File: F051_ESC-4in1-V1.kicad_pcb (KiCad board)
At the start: 4 copper layers, 46 x 55.8 mm, 222 parts, among them J1 Conn_01x02, J11 Conn_01x03, J14 Conn_01x03, J2 Conn_01x10, J3 Conn_01x05, J4 Conn_01x05, J5 Conn_01x05, J6 Conn_01x03, J7 Conn_01x05, J8 Conn_01x03, J9 Conn_01x10, Q1 TPHR8504PL, Q10 TPHR8504PL, Q11 TPHR8504PL, Q12 TPHR8504PL, Q13 TPHR8504PL, Q14 TPHR8504PL, Q15 TPHR8504PL, Q16 TPHR8504PL, Q17 TPHR8504PL, Q18 TPHR8504PL, Q19 TPHR8504PL, Q2 TPHR8504PL, Q20 TPHR8504PL, Q21 TPHR8504PL, Q22 TPHR8504PL, Q23 TPHR8504PL, Q24 TPHR8504PL, Q3 TPHR8504PL, Q4 TPHR8504PL, Q5 TPHR8504PL, Q6 TPHR8504PL, Q7 TPHR8504PL, Q8 TPHR8504PL, Q9 TPHR8504PL, U1 STM32F051K6Ux, U10 FD6288Q, U11 STM32F051K6Ux, U12 FD6288Q, U13 L78L12_SOT89, U14 MP4560_QFN10, U2 FD6288Q, U3 L78L12_SOT89, U4 LP2985-3.3, U5 INA139, U6 FD6288Q, U7 OPA340NA, U8 STM32F051K6Ux, U9 STM32F051K6Ux

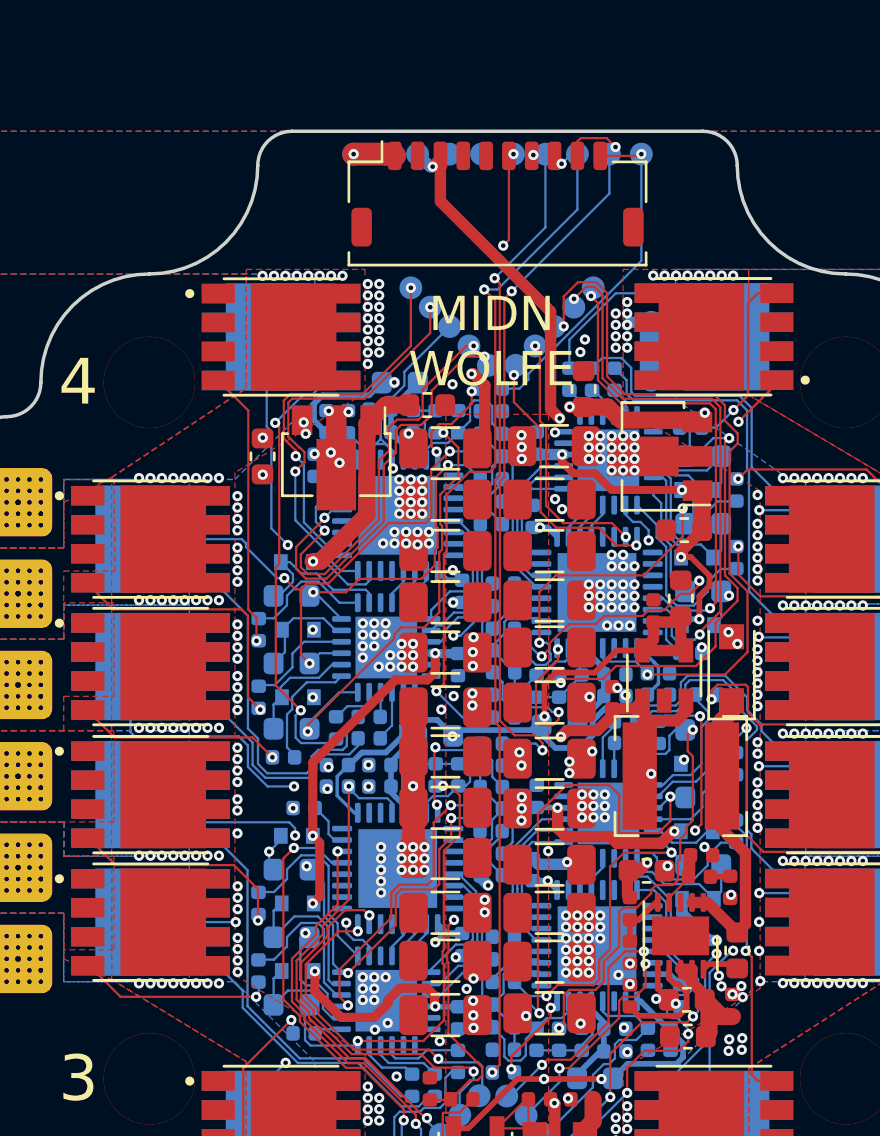
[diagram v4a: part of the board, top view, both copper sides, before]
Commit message: Some graphical additions
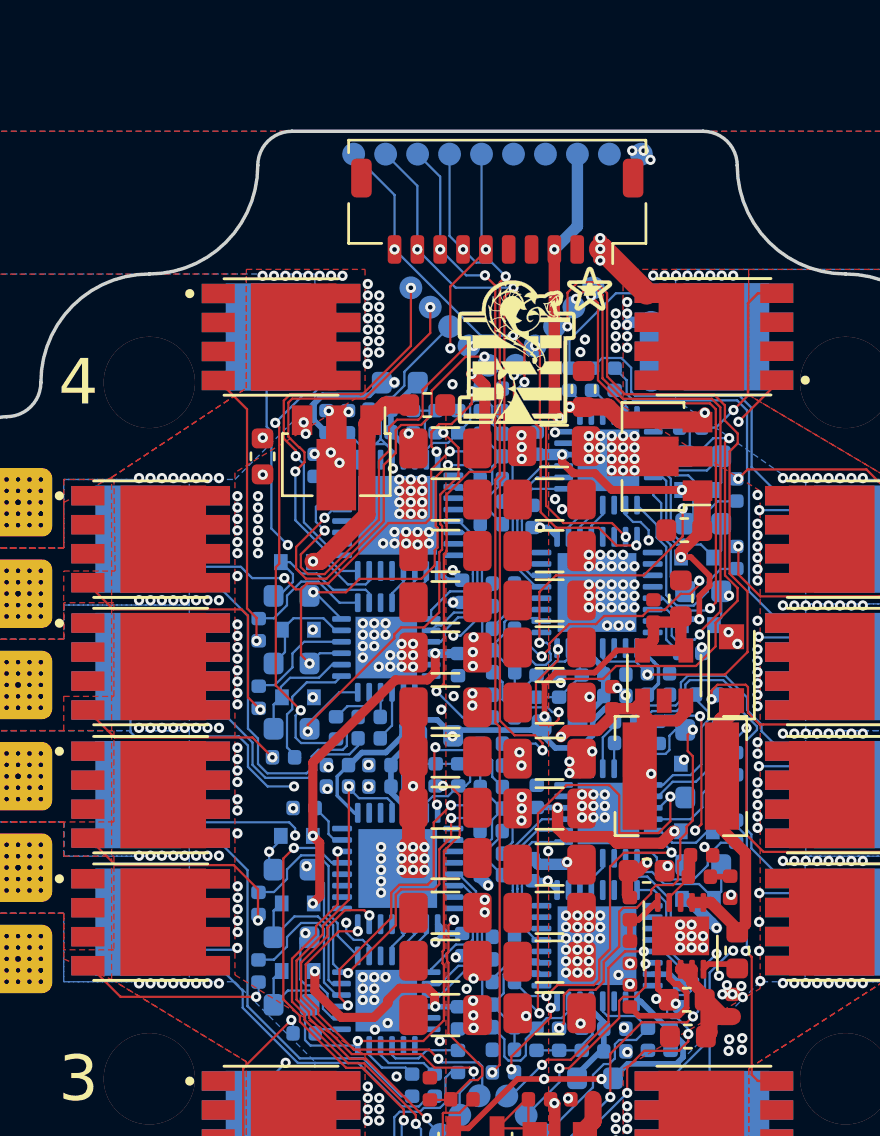
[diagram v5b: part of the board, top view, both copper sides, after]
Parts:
- added G***: LOGO, Footprints:DTOM, F.Cu at (141.6, 72.6)
- moved J2 0.75 mm to (140.0, 65.8), turned to 180 degrees
- turned J9 to 180 degrees
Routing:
- net +5V: track 48.8 -> 45.8 mm
- net /PWM_2: track 31.6 -> 29.9 mm
- net +12V_2: track 29.0 -> 27.9 mm
- net VCC_Shunt: track 20.6 -> 21.6 mm, vias 219 -> 224
- net /PWM_3: track 34.2 -> 33.3 mm
- net /MCU 3/PhaseB: track 26.6 -> 27.2 mm
- net /PWM_4: track 15.1 -> 15.0 mm, vias 1 -> 3
- net GND: vias 334 -> 349
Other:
- board text added: "CLK"
- board text added: "DIO"
- board text added: "NRST"
- board text added: "RX"
- board text added: "TX"

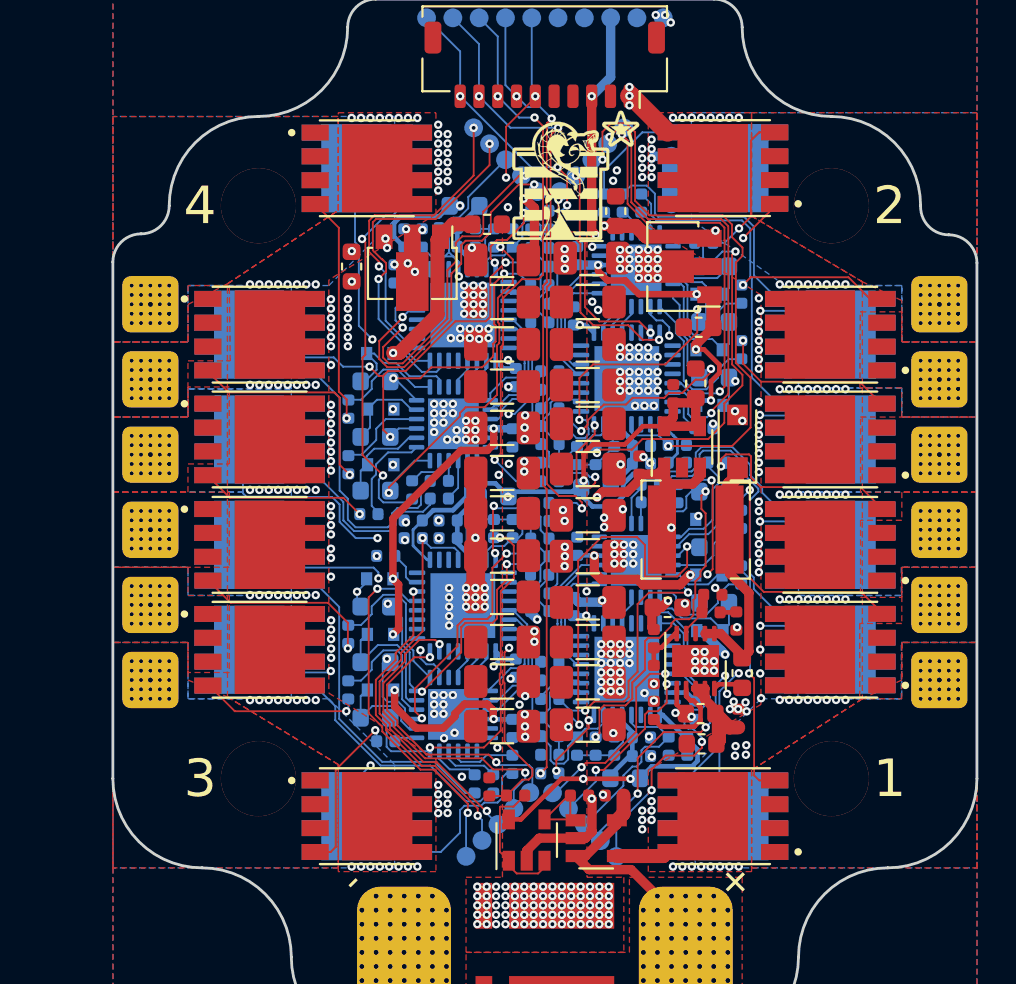
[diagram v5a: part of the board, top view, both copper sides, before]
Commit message: Adjusted some of the fills to match the grid
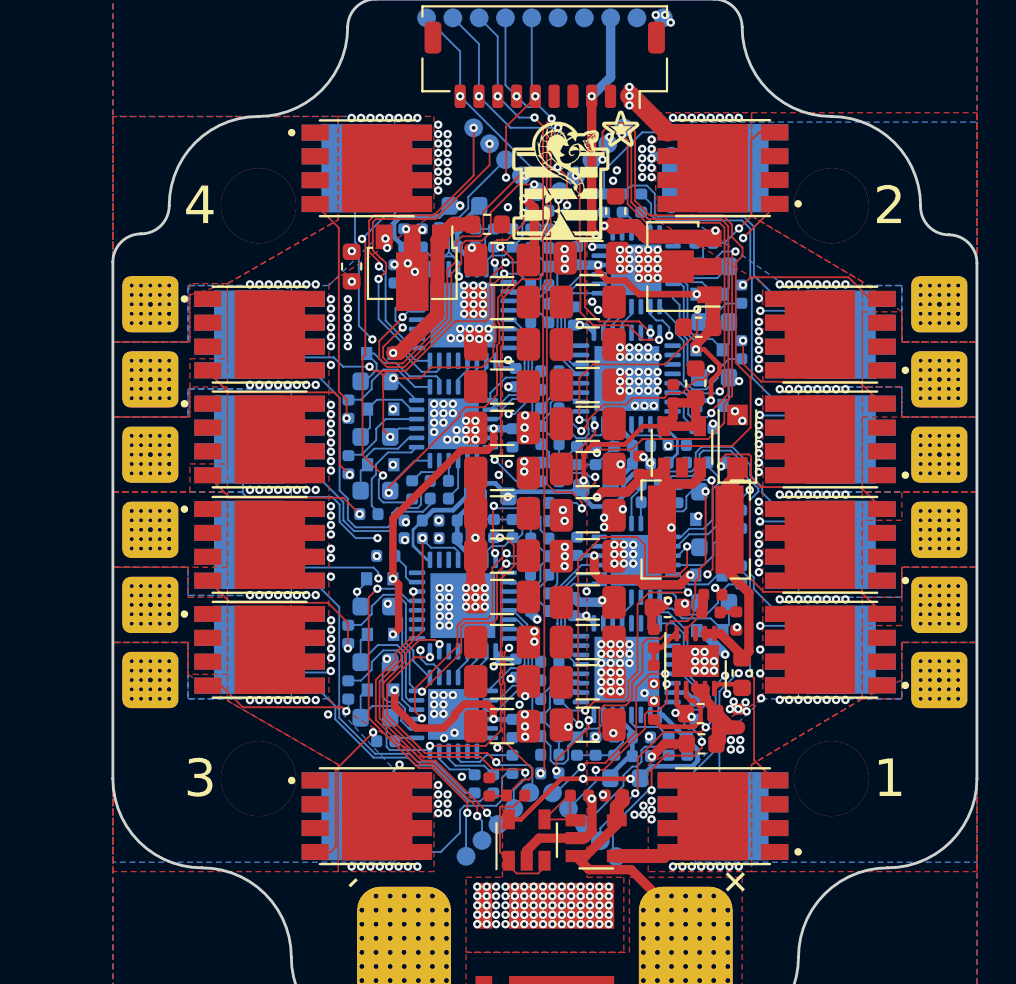
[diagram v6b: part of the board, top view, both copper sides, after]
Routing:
- net GND: track 26.6 -> 28.8 mm, vias 349 -> 354
- net /MCU 3/PhaseC: track 27.9 -> 27.0 mm
- net /MCU 4/PhaseB: track 26.1 -> 26.6 mm
- net VCC_Shunt: vias 224 -> 225
